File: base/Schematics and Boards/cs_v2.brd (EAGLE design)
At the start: 25.4 x 25.4 mm, 80 parts, among them J101 J-JTAG-CORTEX-NEEDLE6, J301 HIROSE-DF40_44-PIN_CONNECTORS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, J302 HIROSE-DF40_30-PIN_CONNECTORS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, Q201 FK3303010L, Q202 FK3303010L, Q203 FK3303010L, Q204 DMG3415UFY4Q-7, U1 AT25SF641-MHB-T, U101 ATSAMD51, U201 COULOMB-MAX17262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

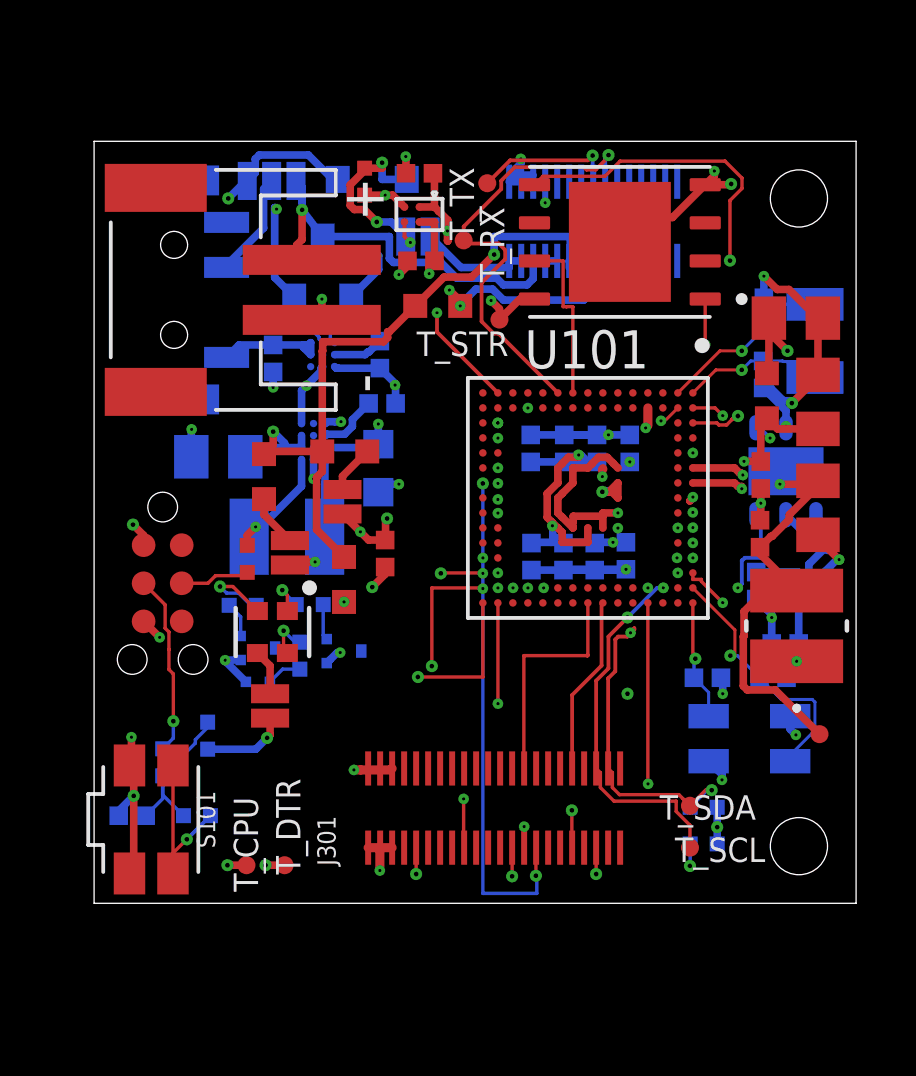
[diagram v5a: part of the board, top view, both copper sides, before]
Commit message: All but DTR/DBG signals hand routed
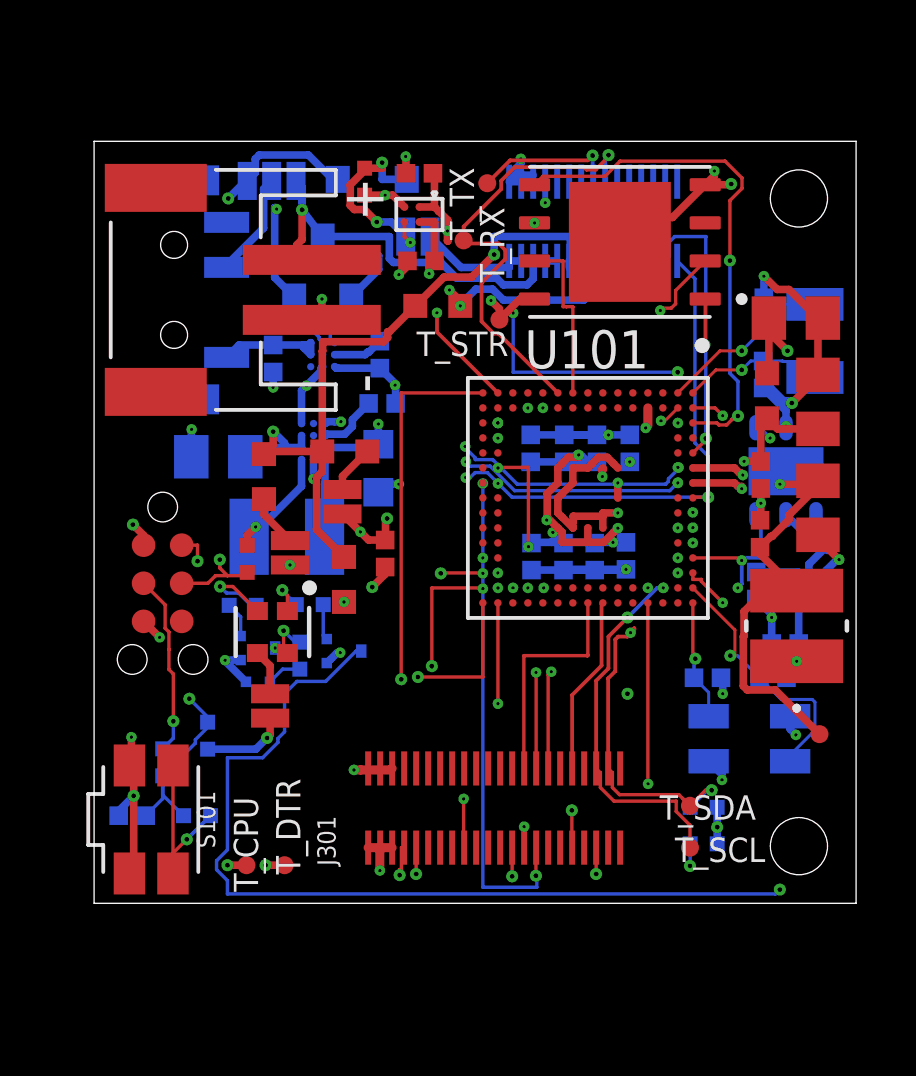
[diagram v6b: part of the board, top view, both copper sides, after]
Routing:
- net LED_G: track 0.03 -> 49.2 mm, vias 2 -> 4
- net LED_B: track 0.02 -> 40.1 mm, vias 2 -> 6
- net NRESET: track 5.91 -> 41.2 mm, vias 2 -> 5
- net DBG_SWDIO: track 0.00 -> 23.4 mm, vias 0 -> 7
- net DBG_SWCLK: track 2.33 -> 24.2 mm, vias 0 -> 8
- net DTR_BUS0_SERCOM0_P0: track 0.00 -> 19.9 mm, vias 0 -> 2
- net STOR_SPI5_SCK: track 0.00 -> 13.0 mm, vias 0 -> 7
- net DTR_BUS3_GPIO0: track 0.00 -> 12.3 mm, vias 0 -> 4
- net DTR_BUS0_GPIO1: track 0.01 -> 12.1 mm, vias 1 -> 6
- net DBG_TRACE_SWO: track 0.45 -> 9.38 mm, vias 2 -> 1
- net STOR_SPI5_MISO: track 0.79 -> 6.96 mm, vias 2 -> 4
- net VDDANA: track 10.9 -> 14.5 mm
- net +3V3_PROC: track 69.7 -> 72.1 mm, vias 22 -> 23
- net +3V3_DTR: track 47.6 -> 46.2 mm, vias 7 -> 9
- net GND: track 150.2 -> 151.1 mm
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
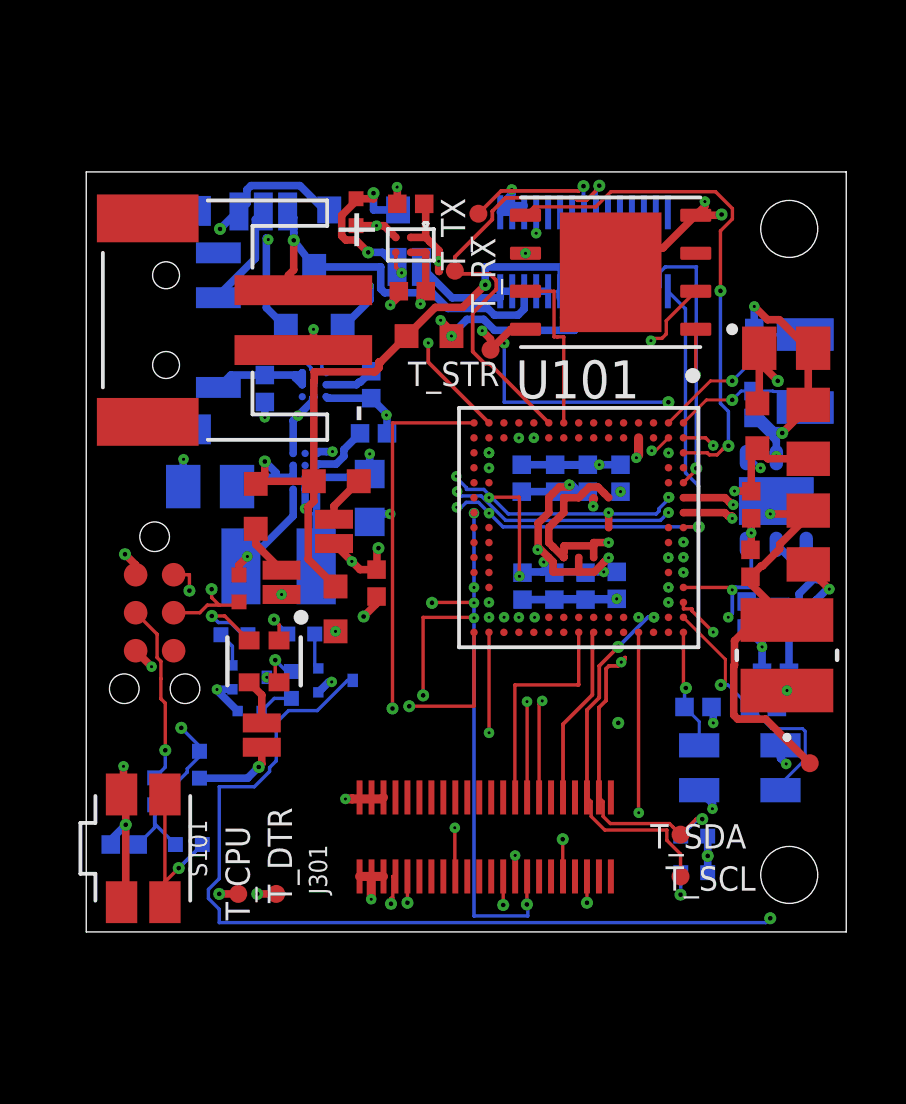
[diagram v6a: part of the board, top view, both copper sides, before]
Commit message: Passed with no DRC errors
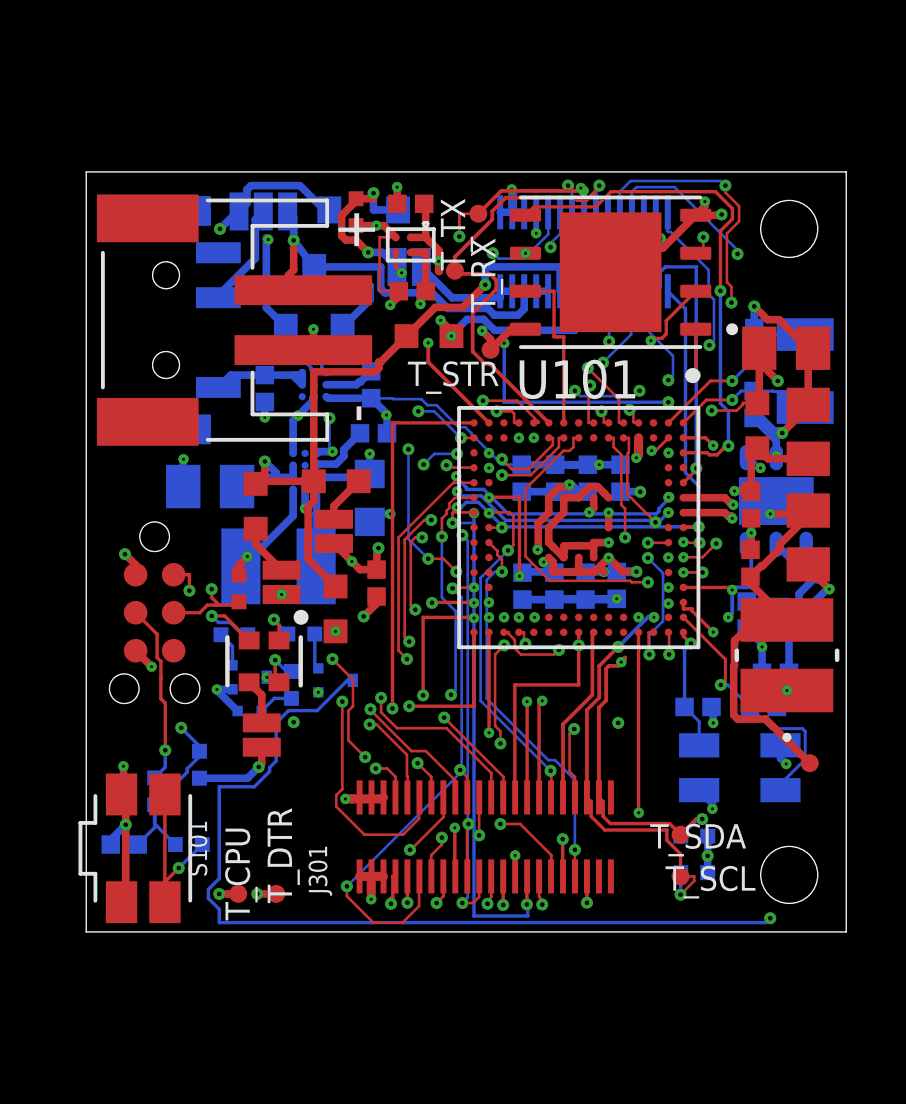
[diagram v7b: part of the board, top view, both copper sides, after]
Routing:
- net DTR_BUS2_AIN0: track 0.00 -> 26.0 mm, vias 0 -> 4
- net DTR_BUS0_SERCOM0_P3: track 0.00 -> 25.5 mm, vias 1 -> 7
- net DTR_BUS0_AIN0: track 0.00 -> 25.2 mm, vias 0 -> 4
- net STOR_WP: track 0.00 -> 25.1 mm, vias 0 -> 2
- net DTR_BUS0_SERCOM0_P2: track 0.00 -> 24.6 mm, vias 0 -> 6
- net DTR_BUS3_AIN0: track 0.00 -> 23.9 mm, vias 0 -> 7
- net DTR_BUS0_AIN1: track 0.00 -> 22.3 mm, vias 0 -> 8
- net DTR_BUS3_AIN1: track 0.00 -> 19.9 mm, vias 0 -> 4
- net DBG_TRACE_D0: track 0.01 -> 19.4 mm, vias 0 -> 5
- net DBG_GPIO1: track 0.04 -> 19.2 mm, vias 2 -> 8
- net +3V3_PROC: track 72.1 -> 91.1 mm, vias 23 -> 28
- net DTR_BUS1_AIN1: track 0.00 -> 18.9 mm, vias 0 -> 5
- net DBG_GPIO0: track 0.70 -> 19.3 mm, vias 2 -> 8
- net DTR_BUS1_AIN0: track 0.00 -> 18.3 mm, vias 0 -> 3
- net DTR_BUS0_SERCOM0_P1: track 0.00 -> 17.8 mm, vias 2 -> 6
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
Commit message: Add GND plugs
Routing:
- net GND: vias 44 -> 116
